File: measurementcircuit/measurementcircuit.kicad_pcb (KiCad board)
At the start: 2 copper layers, 16 parts, among them J2 Conn_01x41

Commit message: Test
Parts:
- added J1: Conn_01x05_Socket, Connector_Pin:Pin_D1.3mm_L10.0mm_W3.5mm_Flat, F.Cu at (83.7, 49.2)
- C1, C2, C3, C4, C5: footprint Capacitor_SMD:CP_Elec_3x5.3 -> Capacitor_THT:CP_Axial_L10.0mm_D4.5mm_P15.00mm_Horizontal
- J2: value Conn_01x41 -> Conn_01x05_Socket; footprint Connector:BJB_Pico_46.110.1001_Receptacle_Horizontal -> Connector_Pin:Pin_D1.3mm_L10.0mm_W3.5mm_Flat
- L1, L2, L3, L4, L5: value 57 μH -> 56 μH; footprint Inductor_SMD:L_6.3x6.3_H3 -> Inductor_THT:L_Axial_L5.0mm_D3.6mm_P10.00mm_Horizontal_Murata_BL01RN1A2A2
- R1, R2, R3, R4, R5: value 1 kΩ -> 100 Ω; footprint Potentiometer_SMD:Potentiometer_ACP_CA6-VSMD_Vertical -> Resistor_THT:R_Axial_DIN0204_L3.6mm_D1.6mm_P5.08mm_Horizontal
- moved C5 40.2 mm to (51.0, 60.8)
- moved C4 40.0 mm to (51.0, 54.3)
- moved C1 40.0 mm to (51.0, 34.7)
- moved C3 40.0 mm to (51.0, 47.7)
- moved C2 40.0 mm to (51.0, 41.2)
- moved R5 23.4 mm to (82.4, 45.3)
- moved J2 21.4 mm to (83.7, 53.9)
- moved L5 21.0 mm to (69.3, 54.3)
- moved L4 19.1 mm to (69.3, 49.2)
- moved R4 19.0 mm to (82.4, 42.2)
- moved L3 17.3 mm to (69.3, 44.0)
- moved L2 15.9 mm to (69.3, 38.9)
- moved R3 15.0 mm to (82.4, 39.0)
- moved L1 14.8 mm to (69.3, 33.7)
- moved R2 11.7 mm to (82.4, 35.9)
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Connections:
- R1 pad 1: Net-(J2-Pin_1) -> Net-(J2-Pin_5)
- R5 pad 1: Net-(J2-Pin_5) -> Net-(J2-Pin_1)

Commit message: Only missing POT
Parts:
- removed R1, R2, R3, R4, R5: 100 Ω, Resistor_THT:R_Axial_DIN0204_L3.6mm_D1.6mm_P5.08mm_Horizontal
- added J10: Conn_01x02, Connector_PinHeader_2.54mm:PinHeader_1x02_P2.54mm_Vertical, F.Cu at (134.7, 116.7)
- added J11: Conn_01x02, Connector_PinHeader_2.54mm:PinHeader_1x02_P2.54mm_Vertical, F.Cu at (139.3, 116.7)
- added J12: Conn_01x02, Connector_PinHeader_2.54mm:PinHeader_1x02_P2.54mm_Vertical, F.Cu at (143.9, 116.7)
- added J3: 2604-3102, Senior_Design:CONN2_2604-3102_WAG, F.Cu at (115.1, 69.0)
- added J4: 2604-3102, Senior_Design:CONN2_2604-3102_WAG, F.Cu at (130.5, 69.0)
- added J5: 2604-3102, Senior_Design:CONN2_2604-3102_WAG, F.Cu at (145.9, 69.0)
- added J6: 2604-3102, Senior_Design:CONN2_2604-3102_WAG, F.Cu at (161.2, 69.0)
- added J7: 2604-3102, Senior_Design:CONN2_2604-3102_WAG, F.Cu at (176.6, 69.0)
- added J8: Conn_01x02, Connector_PinHeader_2.54mm:PinHeader_1x02_P2.54mm_Vertical, F.Cu at (125.6, 116.7)
- added J9: Conn_01x02, Connector_PinHeader_2.54mm:PinHeader_1x02_P2.54mm_Vertical, F.Cu at (130.1, 116.7)
- added RV1: 1kΩ, Potentiometer_THT:Potentiometer_ACP_CA9-V10_Vertical, F.Cu at (111.3, 89.8)
- added RV2: 1kΩ, Potentiometer_THT:Potentiometer_ACP_CA9-V10_Vertical, F.Cu at (111.3, 101.2)
- added RV3: 1kΩ, Potentiometer_THT:Potentiometer_ACP_CA9-V10_Vertical, F.Cu at (111.3, 112.6)
- added RV4: 1kΩ, Potentiometer_THT:Potentiometer_ACP_CA9-V10_Vertical, F.Cu at (111.3, 123.9)
- added RV5: 1kΩ, Potentiometer_THT:Potentiometer_ACP_CA9-V10_Vertical, F.Cu at (111.3, 135.3)
- C1, C2, C3, C4, C5: value 10 pF -> 10pF; footprint Capacitor_THT:CP_Axial_L10.0mm_D4.5mm_P15.00mm_Horizontal -> Capacitor_SMD:C_0805_2012Metric
- J1: value Conn_01x05_Socket -> 2601-3110; footprint Connector_Pin:Pin_D1.3mm_L10.0mm_W3.5mm_Flat -> Senior_Design:CONN10_2601-3110_WAG
- J2: value Conn_01x05_Socket -> 2604-3106; footprint Connector_Pin:Pin_D1.3mm_L10.0mm_W3.5mm_Flat -> Senior_Design:CONN6_2604-3106_WAG
- L1, L2, L3, L4, L5: value 56 μH -> 56μH; footprint Inductor_THT:L_Axial_L5.0mm_D3.6mm_P10.00mm_Horizontal_Murata_BL01RN1A2A2 -> Inductor_SMD:L_0805_2012Metric
- moved C1 115.6 mm to (125.5, 123.1)
- moved C2 112.9 mm to (125.5, 126.1)
- moved C3 110.3 mm to (125.5, 129.1)
- moved L1 107.9 mm to (130.0, 122.9)
- moved C4 107.7 mm to (125.5, 132.1)
- moved L2 105.9 mm to (130.0, 125.7)
- moved C5 105.2 mm to (125.5, 135.1)
- moved L3 103.9 mm to (130.0, 128.4)
- moved L4 102.0 mm to (130.0, 131.2)
- moved L5 100.1 mm to (130.0, 133.9)
- moved J2 65.9 mm to (129.0, 101.8)
- moved J1 59.4 mm to (128.8, 87.9)
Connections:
- C1 pad 1: Net-(J1-Pin_1) -> Net-(C1-Pad1)
- C2 pad 1: Net-(J1-Pin_2) -> Net-(C2-Pad1)
- J1 pad 1: Net-(J1-Pin_1) -> Net-(J1-1_1)
- J2 pad 1: Net-(J2-Pin_1) -> Net-(J2-1_1)
- L1 pad 1: Net-(L1-Pad1) -> Net-(J2-6_1)
- L1 pad 2: Net-(J1-Pin_1) -> Net-(C2-Pad1)
- L2 pad 1: Net-(L2-Pad1) -> Net-(J2-5_1)
- L2 pad 2: Net-(J1-Pin_2) -> Net-(C1-Pad1)
- L3 pad 1: Net-(L3-Pad1) -> Net-(J2-4_1)
- L4 pad 1: Net-(L4-Pad1) -> Net-(J2-3_1)
- L5 pad 1: Net-(L5-Pad1) -> Net-(J2-2_1)

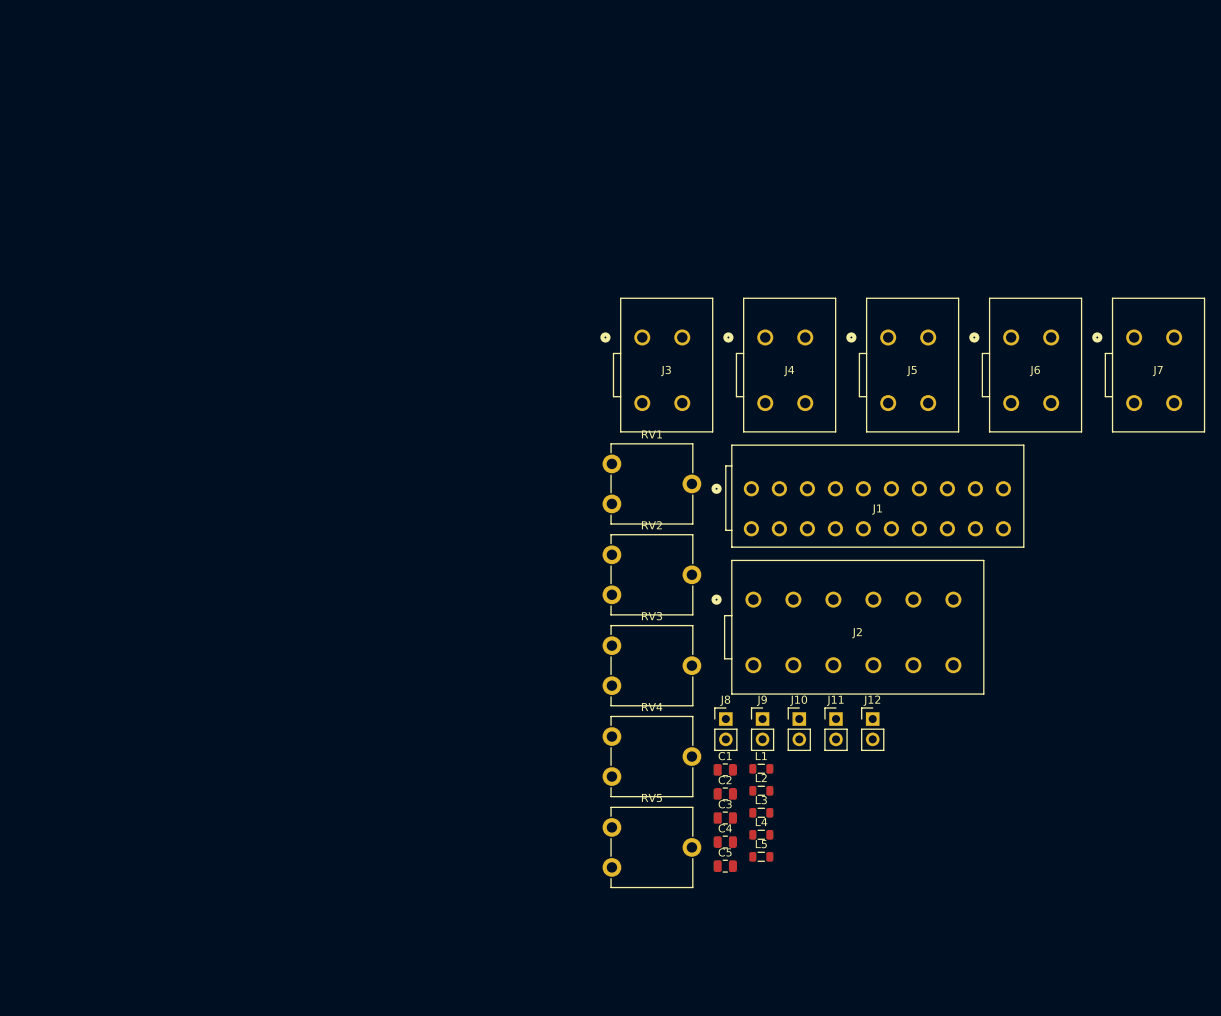
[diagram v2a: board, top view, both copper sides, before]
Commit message: Did some of the PCB layout
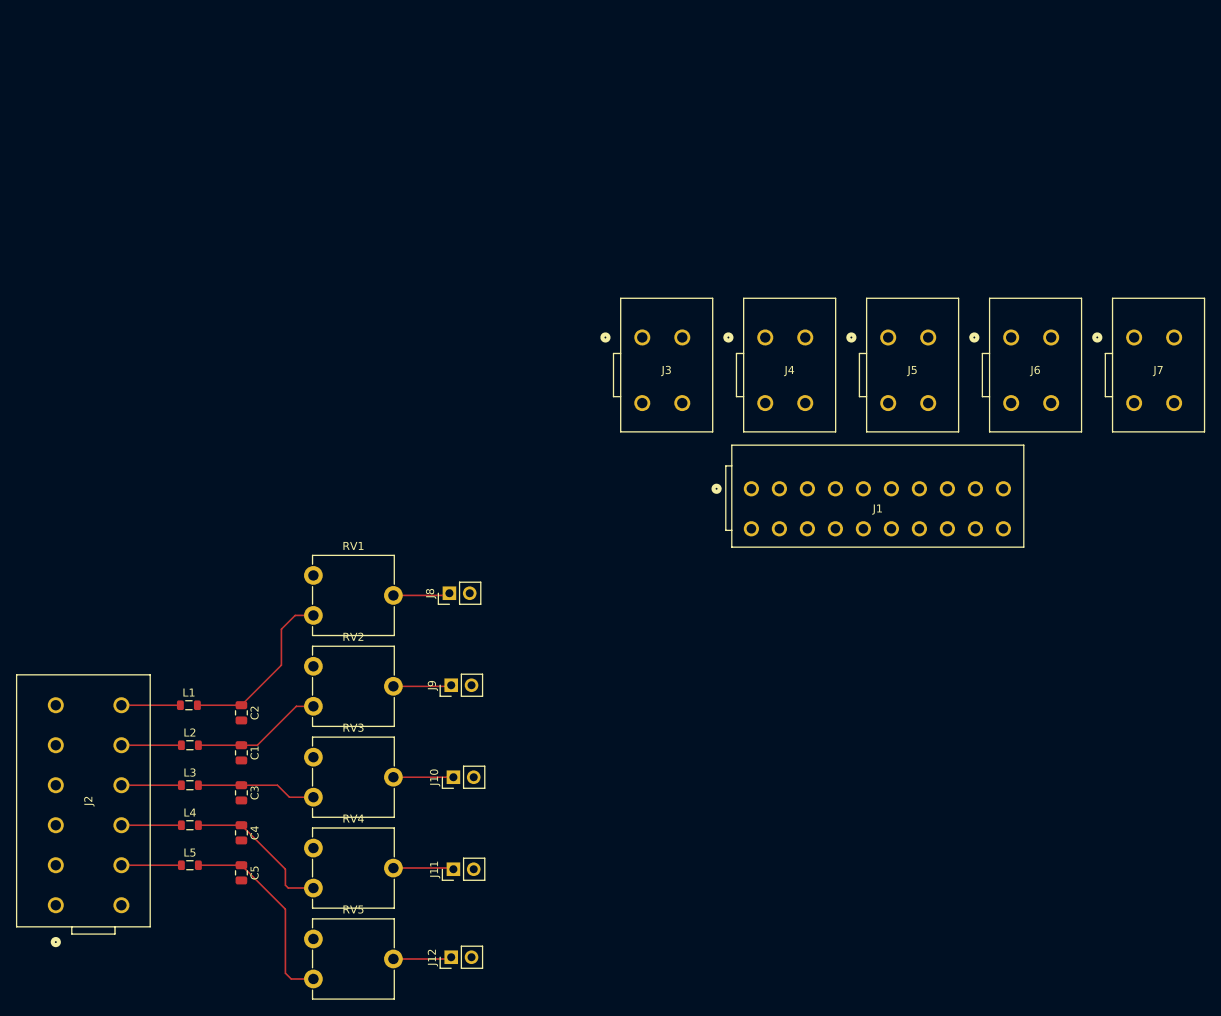
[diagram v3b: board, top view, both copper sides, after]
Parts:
- moved J2 95.2 mm to (41.8, 140.0), turned to 90 degrees
- moved L1 72.0 mm to (58.4, 115.0)
- moved L2 71.6 mm to (58.6, 120.0)
- moved L3 71.5 mm to (58.6, 125.0)
- moved L4 71.4 mm to (58.6, 130.0)
- moved L5 71.4 mm to (58.6, 135.0)
- moved C2 61.3 mm to (65.0, 116.0), turned to -90 degrees
- moved C3 60.6 mm to (65.0, 126.0), turned to -90 degrees
- moved C1 60.5 mm to (65.0, 121.0), turned to -90 degrees
- moved J12 60.5 mm to (91.2, 146.5), turned to 90 degrees
- moved C4 60.5 mm to (65.0, 130.9), turned to -90 degrees
- moved C5 60.5 mm to (65.0, 135.9), turned to -90 degrees
- moved J11 51.4 mm to (91.5, 135.5), turned to 90 degrees
- moved J10 43.8 mm to (91.5, 124.0), turned to 90 degrees
- moved RV1 39.8 mm to (74.0, 103.8)
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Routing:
- net Net-(C5-Pad1): track 0.00 -> 24.9 mm
- net Net-(C2-Pad1): track 0.00 -> 21.8 mm
- net Net-(C4-Pad1): track 0.00 -> 18.8 mm
- net Net-(C1-Pad1): track 0.00 -> 16.4 mm
- net Net-(C3-Pad1): track 0.00 -> 15.0 mm
- net Net-(J11-Pin_1): track 0.00 -> 7.56 mm
- net Net-(J10-Pin_1): track 0.00 -> 7.50 mm
- net Net-(J2-5_1): track 0.00 -> 7.50 mm
- net Net-(J2-4_1): track 0.00 -> 7.50 mm
- net Net-(J2-3_1): track 0.00 -> 7.50 mm
- net Net-(J2-2_1): track 0.00 -> 7.50 mm
- net Net-(J2-6_1): track 0.00 -> 7.38 mm
- net Net-(J12-Pin_1): track 0.00 -> 7.31 mm
- net Net-(J9-Pin_1): track 0.00 -> 7.28 mm
- net Net-(J8-Pin_1): track 0.00 -> 7.11 mm
